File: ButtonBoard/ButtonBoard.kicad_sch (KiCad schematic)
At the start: 17 parts, among them J1 Conn_01x15_Socket, J2 Conn_01x15_Socket, J3 START, J4 PAUSE, J5 RESET, J6 TIME_SEL, J7 BUZZER, J8 Conn_01x06_Pin, SW1 START, SW2 PAUSE, SW3 RESET, SW4 TIME_SEL, SW5 BUZZER

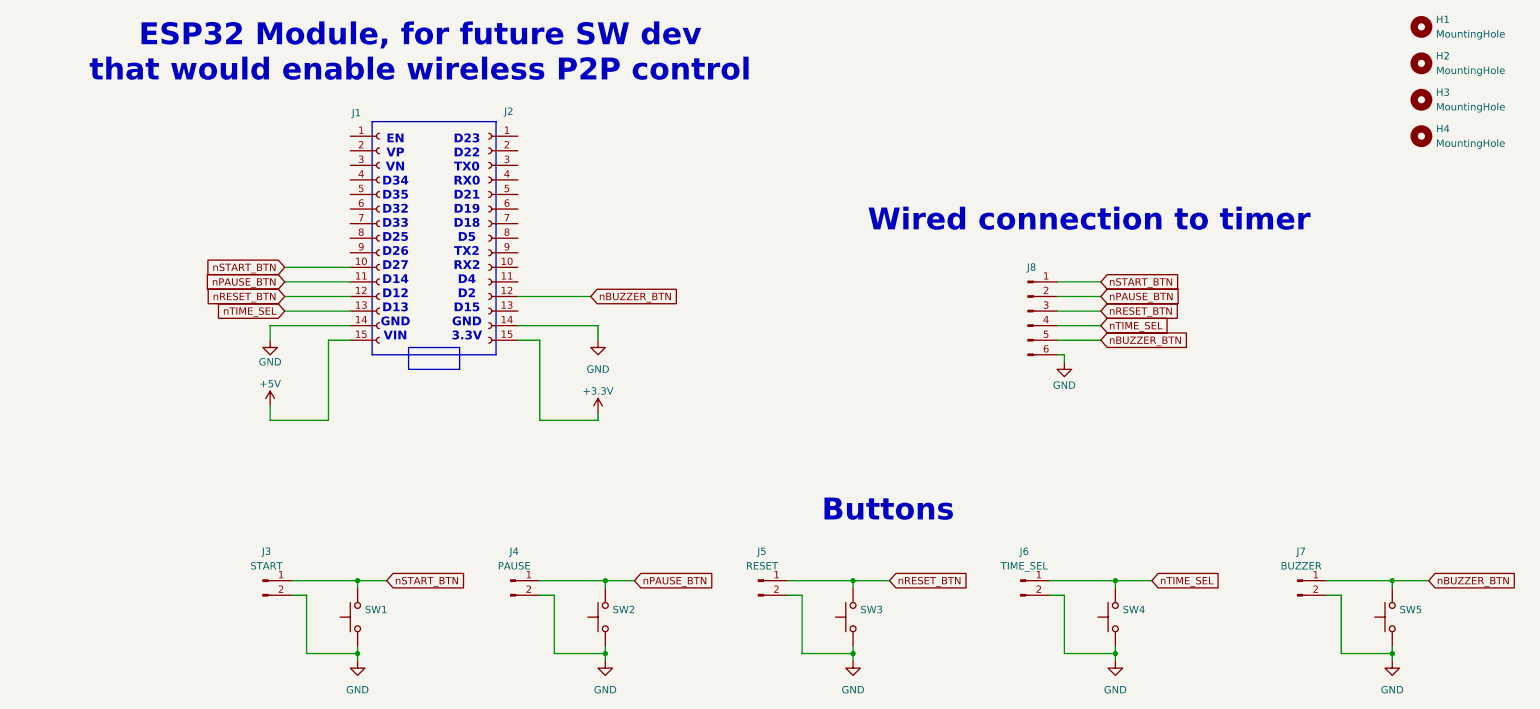
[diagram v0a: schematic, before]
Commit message: update controller board to include esp8266
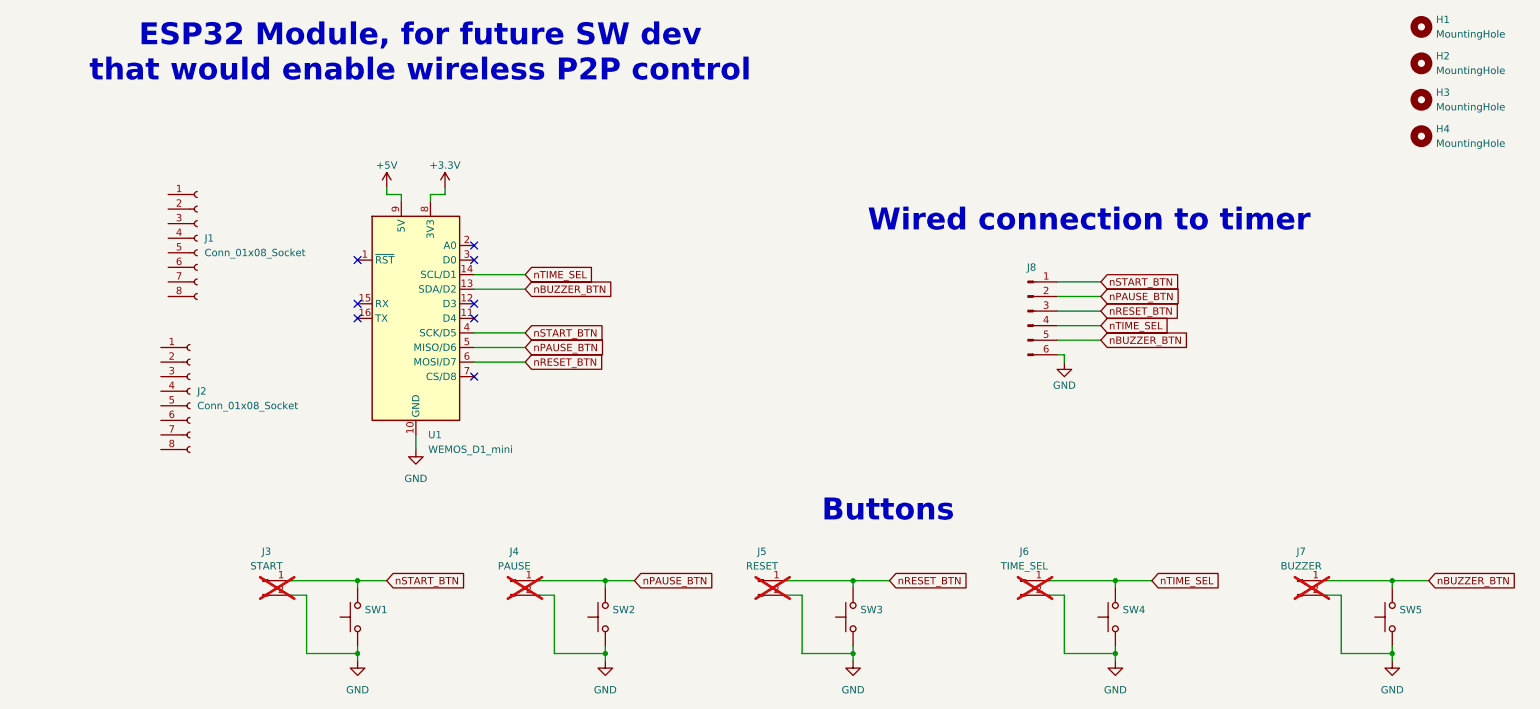
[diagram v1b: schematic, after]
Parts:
- removed J1, J2: Conn_01x15_Socket, Connector_PinSocket_2.54mm:PinSocket_1x15_P2.54mm_Vertical, symbol Connector:Conn_01x15_Socket
- added J1, J2: Conn_01x08_Socket, Connector_PinHeader_2.54mm:PinHeader_1x08_P2.54mm_Vertical, symbol Connector:Conn_01x08_Socket
- added U1: WEMOS_D1_mini, RF_Module:WEMOS_D1_mini_light, symbol RF_Module:WEMOS_D1_mini
- J3, J4, J5, J6, J7: now not fitted; now left out of the parts list
- SW1, SW2, SW3, SW4, SW5: LCSC C5377619 -> C2888699
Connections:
- net +3.3V: now also U1.8 (3V3)
- net +5V: now also U1.9 (5V)
- net GND: now also U1.10 (GND)
- net nBUZZER_BTN: now also U1.13 (SDA/D2)
- net nPAUSE_BTN: now also U1.5 (MISO/D6)
- net nRESET_BTN: now also U1.6 (MOSI/D7)
- net nSTART_BTN: now also U1.4 (SCK/D5)
- net nTIME_SEL: now also U1.14 (SCL/D1)
- no-connect marks 0 -> 8
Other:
- note removed: "D23 D22 TX0 RX0 D21 D19 D18 D5 TX2 RX2 D4 D2 D15 GND 3.3V"
- note removed: "EN VP VN D34 D35 D32 D33 D25 D26 D27 D14 D12 D13 GND VIN"

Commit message: finish controller board and prod files
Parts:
- removed J8: Conn_01x06_Pin, Connector_JST:JST_EH_S6B-EH_1x06_P2.50mm_Horizontal, symbol Connector:Conn_01x06_Pin
- removed U1: WEMOS_D1_mini, RF_Module:WEMOS_D1_mini_light, symbol RF_Module:WEMOS_D1_mini
- added D1: Red, LED_SMD:LED_0603_1608Metric, symbol Device:LED
- added J9: WAGO, WAGO_2060-452_998-404:2060-452_998-404, symbol Connector:Conn_01x02_Socket
- added R1: 470, Resistor_SMD:R_0603_1608Metric, symbol Device:R_US
- J1, J2: footprint Connector_PinHeader_2.54mm:PinHeader_1x08_P2.54mm_Vertical -> Connector_PinSocket_2.54mm:PinSocket_1x08_P2.54mm_Vertical
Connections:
- net +3.3V: now also J1.8 (Pin_8)
- net +5V: now also J2.8 (Pin_8), J9.2 (Pin_2)
- net GND: now also J2.7 (Pin_7), D1.1 (K), J9.1 (Pin_1)
- net nBUZZER_BTN: now also J2.3 (Pin_3)
- net nPAUSE_BTN: now also J1.5 (Pin_5)
- net nRESET_BTN: now also J1.4 (Pin_4)
- net nSTART_BTN: now also J1.6 (Pin_6)
- net nTIME_SEL: now also J2.4 (Pin_4)
- net at J1.3 (Pin_3): now also R1.2
- new net: D1.2 (A), R1.1
- no-connect marks 8 -> 7
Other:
- note added: "ANTENNA"
- note added: "ESP8266 Module"
- note added: "RST A0 D0 D5 D6 D7 D8 3.3V"
- note added: "TX RX D1 D2 D3 D4 G 5V"
- note added: "WAGO Battery Input"
- note removed: "ESP32 Module, for future SW dev that would enable wireless P2P control"
- note removed: "Wired connection to timer"
- moved on the sheet: J1, J2
